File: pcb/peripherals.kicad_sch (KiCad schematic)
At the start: 30 parts, among them J2 Conn_01x24_MountingPin, J3 Conn_02x10_Odd_Even, U4 TLV74328PDBVR, U5 NRF24L01_Breakout, U6 TLV74315PDBVR, U7 BMI270, U8 HYCW110-TF10-180B

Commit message: [pcb] invented the cutting edge, extremely innovative monke and ddg connectors
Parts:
- removed J3: Conn_02x10_Odd_Even, Connector_PinHeader_2.54mm:PinHeader_2x10_P2.54mm_Vertical, symbol Connector_Generic:Conn_02x10_Odd_Even
- added J3: Conn_02x04_Odd_Even, symbol Connector_Generic:Conn_02x04_Odd_Even
- added J4: Conn_02x05_Odd_Even, symbol Connector_Generic:Conn_02x05_Odd_Even
- added SW5: SW_Slide_DPDT, symbol Switch:SW_Slide_DPDT
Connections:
- net +3.3V: now also J3.2 (Pin_2), J4.2 (Pin_2)
- net GND: now also J3.4 (Pin_4), J4.4 (Pin_4)
- net IMU_SCL: now also SW5.1 (A)
- net IMU_SDA: now also SW5.6 (C)
- net RST: now also J3.8 (Pin_8)
- net SPI2_CLK: now also J4.10 (Pin_10)
- net SPI2_MISO: now also SW5.3 (C)
- net SPI2_MOSI: now also SW5.4 (A)
- net TCLK: now also J3.7 (Pin_7)
- net TDI: now also J3.3 (Pin_3)
- net TDO: now also J3.6 (Pin_6)
- net TMS: now also J3.5 (Pin_5)
- net TRST: now also J3.1 (Pin_1)
- new net DDG_MAGIC_1: J4.1 (Pin_1)
- new net DDG_MAGIC_2: J4.3 (Pin_3)
- new net DDG_MAGIC_3: J4.5 (Pin_5)
- new net DDG_MAGIC_4: J4.7 (Pin_7)
- new net DDG_MAGIC_5: J4.9 (Pin_9)
- new net MISO_SCL: J4.6 (Pin_6), SW5.2 (B)
- new net MOSI_SDA: J4.8 (Pin_8), SW5.5 (B)
- no-connect marks 13 -> 10
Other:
- note added: "DUCKDUCKGOOSE (Digital Unified Centralized Kibibit Device Universal Coding Knowledge Generic Operable Objective Service Extensible) Connector"
- note added: "MONKE (Magic Overengineered Nonsense for Kernel Experiments) Connector"
- note removed: "JTAG Connector"
- moved on the sheet: C29, C30, C32, R16, R17, R18, R19, R20, R21, R23, R24, U7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

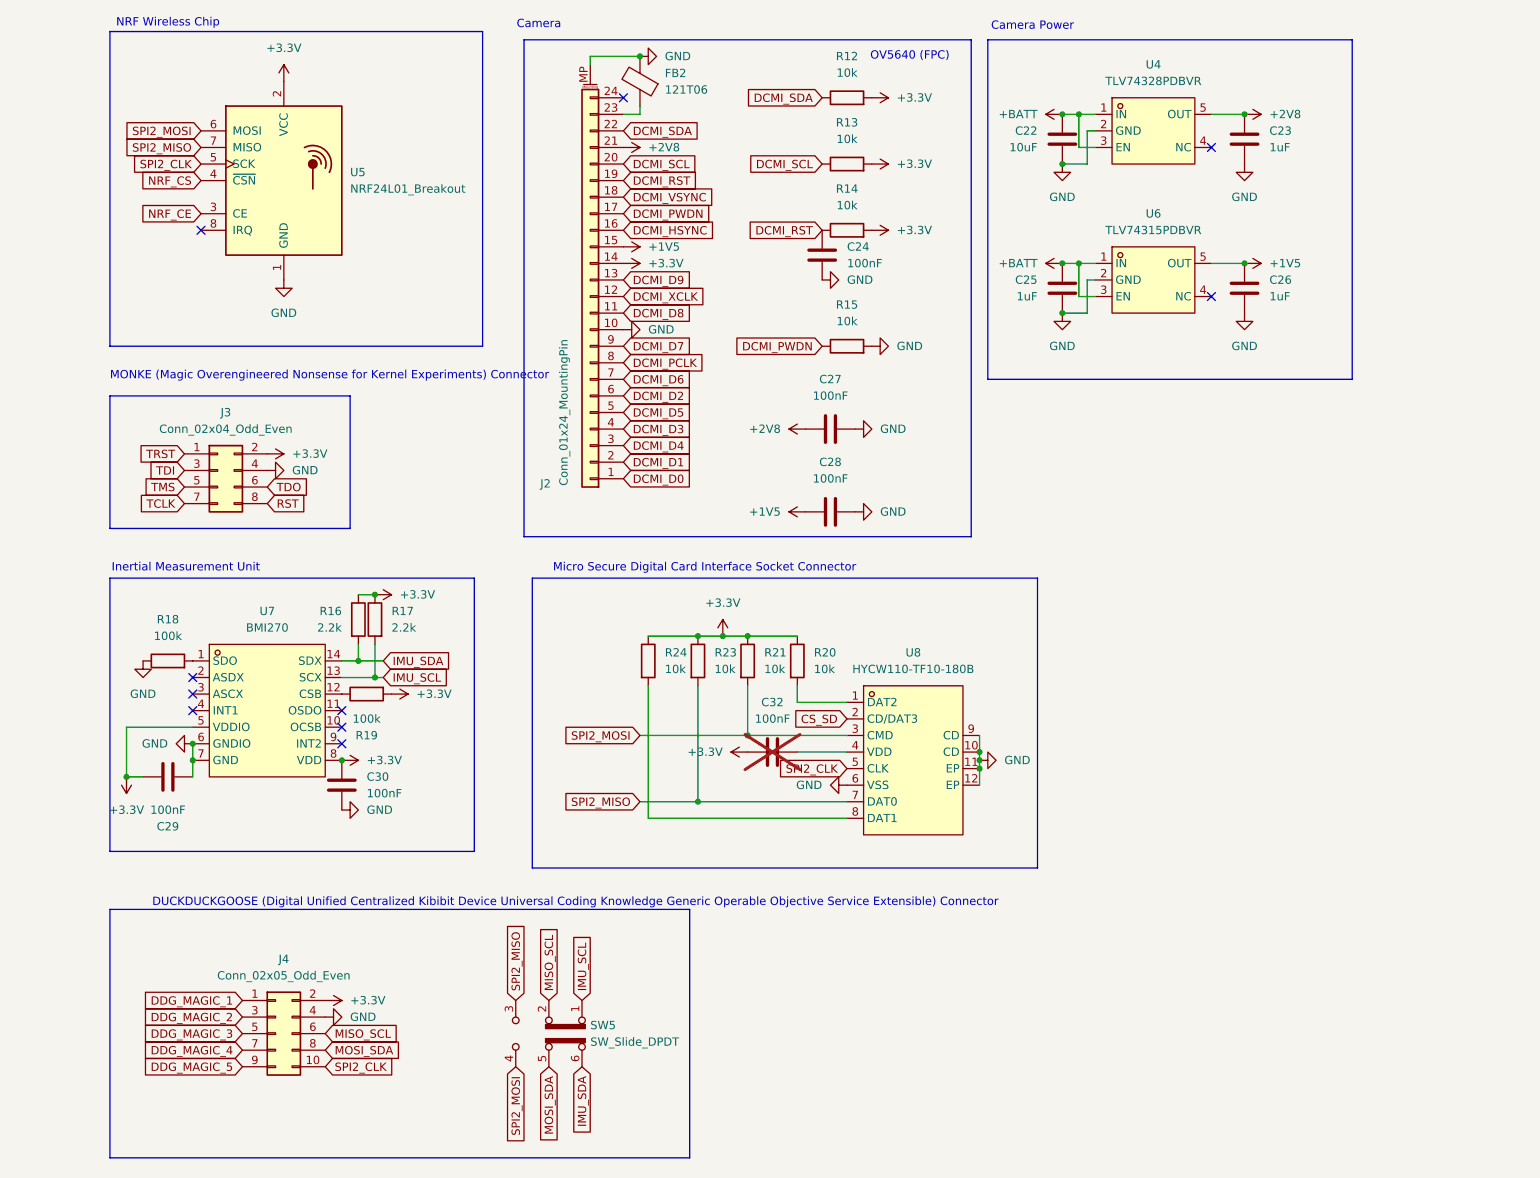
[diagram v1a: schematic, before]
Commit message: [pcb] changed switches to optimize pcb layout
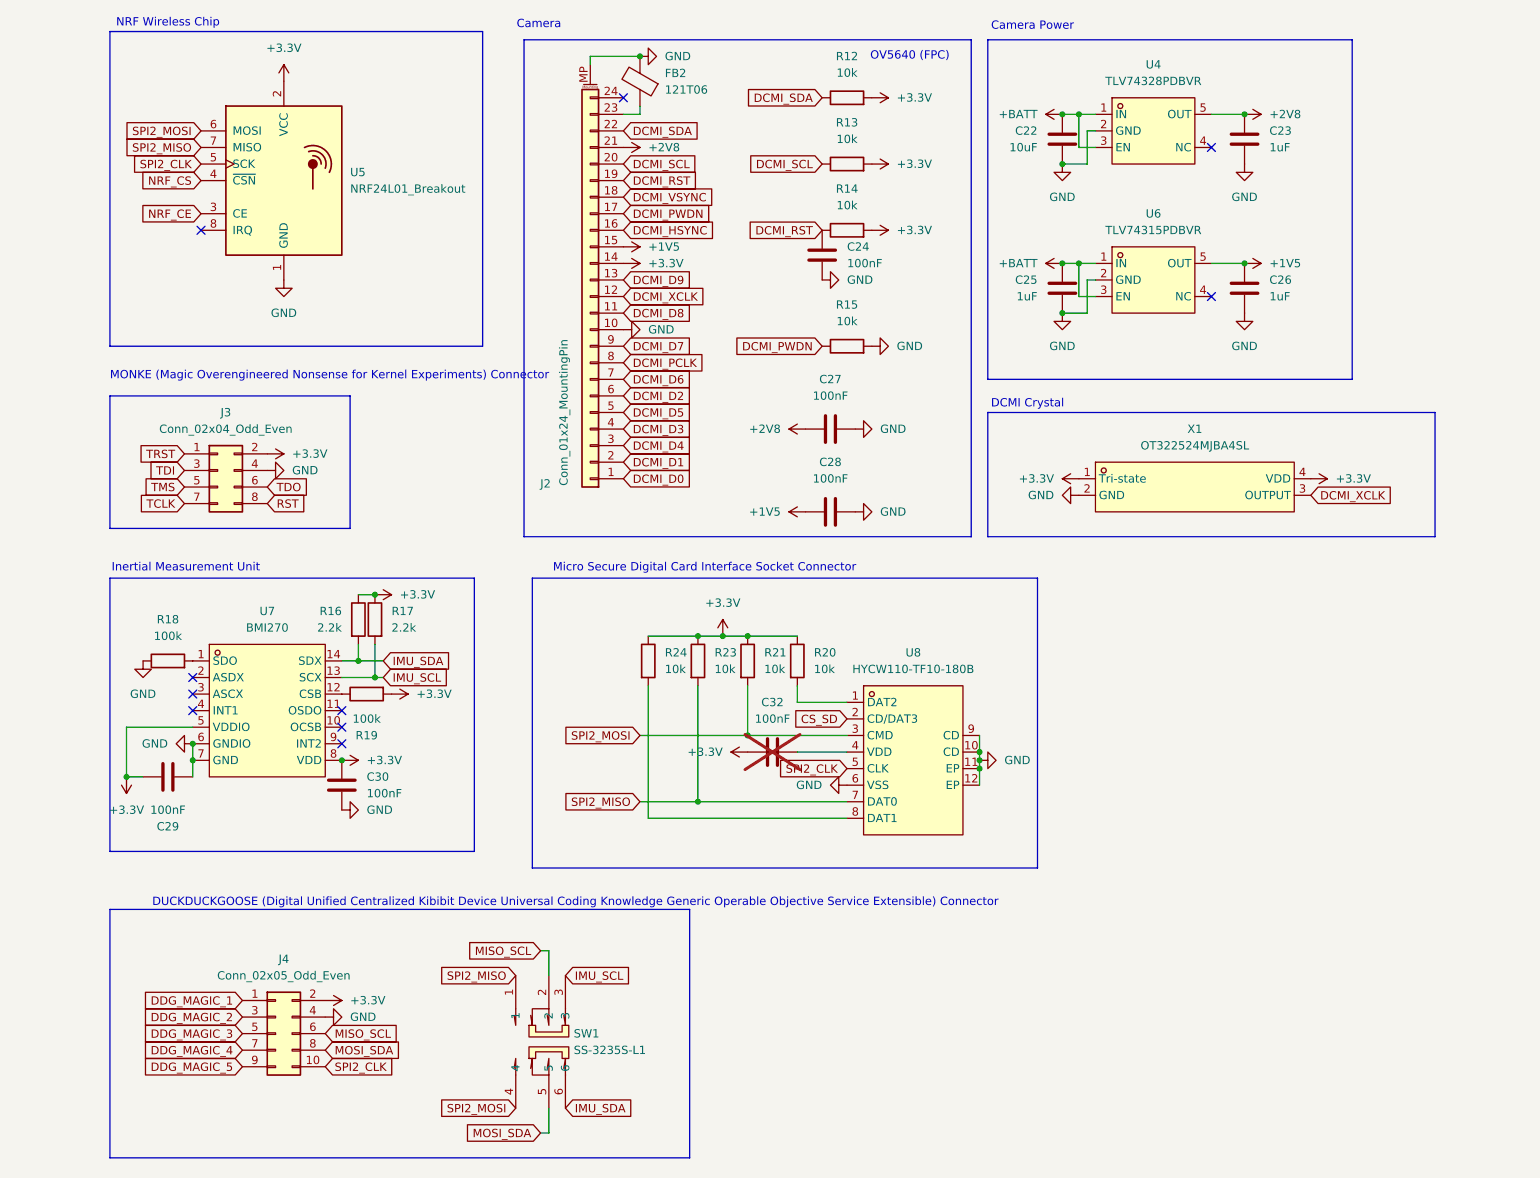
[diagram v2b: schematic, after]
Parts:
- removed SW5: SW_Slide_DPDT, symbol Switch:SW_Slide_DPDT
- added SW1: SS-3235S-L1, lcsc:SW-SMD_SS-3235S-LX, symbol lcsc:SS-3235S-L1
- added X1: OT322524MJBA4SL, Crystal:Crystal_SMD_3225-4Pin_3.2x2.5mm_HandSoldering, symbol lcsc:OT322524MJBA4SL
- J3: footprint (none) -> Connector_PinHeader_2.54mm:PinHeader_2x04_P2.54mm_Vertical
- J4: footprint (none) -> Connector_PinHeader_2.54mm:PinHeader_2x05_P2.54mm_Vertical
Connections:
- net +3.3V: now also X1.1 (Tri-state), X1.4 (VDD)
- net DCMI_XCLK: now also X1.3 (OUTPUT)
- net GND: now also X1.2 (GND)
- net IMU_SCL: now also SW1.3
- net IMU_SDA: now also SW1.6
- net MISO_SCL: now also SW1.2
- net MOSI_SDA: now also SW1.5
- net SPI2_MISO: now also SW1.1
- net SPI2_MOSI: now also SW1.4
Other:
- note added: "DCMI Crystal"

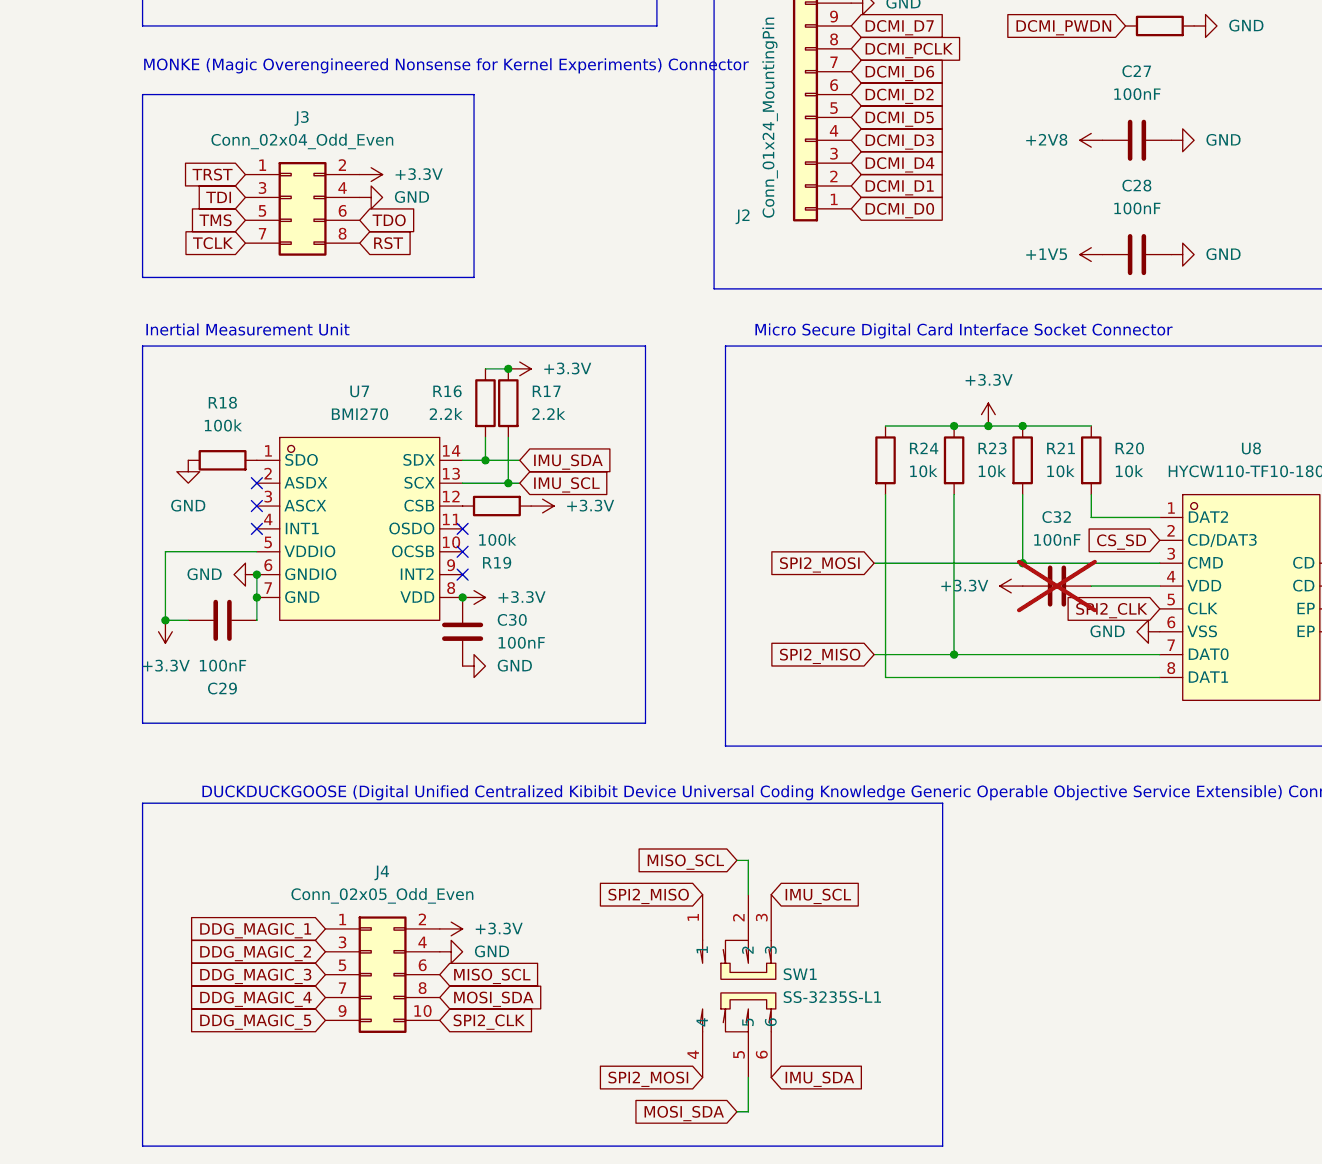
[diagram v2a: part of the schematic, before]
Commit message: [pcb] finish routing
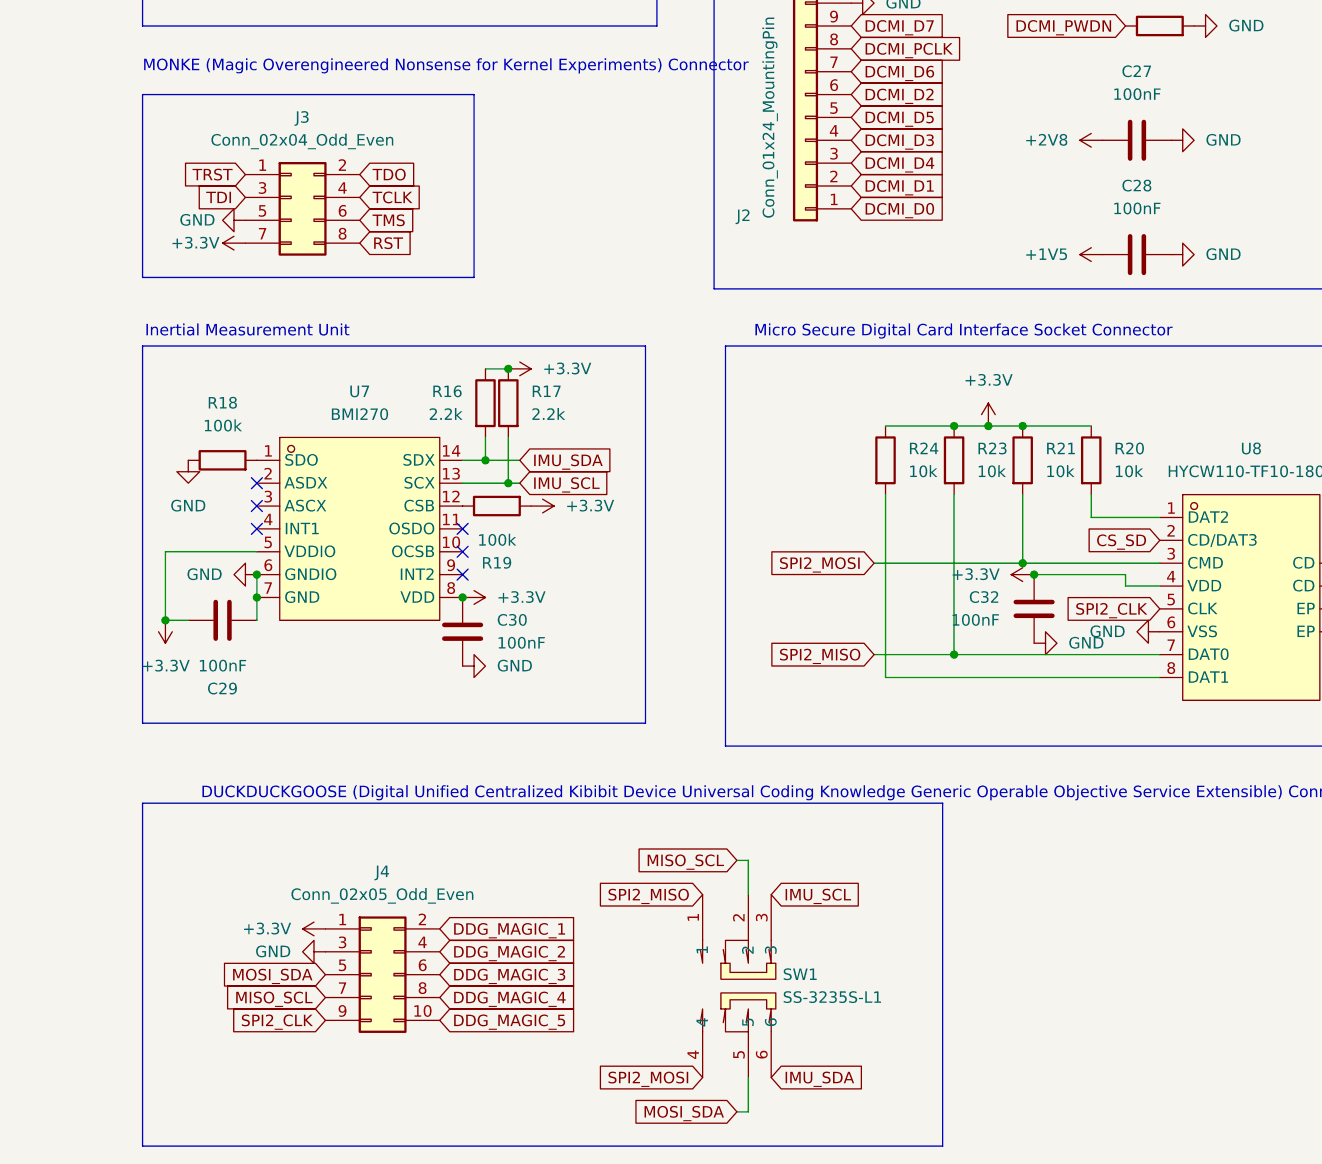
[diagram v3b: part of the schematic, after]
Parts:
- C32: now fitted
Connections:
- net +3.3V: now also J3.7 (Pin_7), J4.1 (Pin_1), U8.4 (VDD); no longer J3.2 (Pin_2), J4.2 (Pin_2)
- net DDG_MAGIC_1: now also J4.2 (Pin_2); no longer J4.1 (Pin_1)
- net DDG_MAGIC_2: now also J4.4 (Pin_4); no longer J4.3 (Pin_3)
- net DDG_MAGIC_3: now also J4.6 (Pin_6); no longer J4.5 (Pin_5)
- net DDG_MAGIC_4: now also J4.8 (Pin_8); no longer J4.7 (Pin_7)
- net DDG_MAGIC_5: now also J4.10 (Pin_10); no longer J4.9 (Pin_9)
- net GND: now also C32.2, J3.5 (Pin_5), J4.3 (Pin_3); no longer J3.4 (Pin_4), J4.4 (Pin_4)
- net MISO_SCL: now also J4.7 (Pin_7); no longer J4.6 (Pin_6)
- net MOSI_SDA: now also J4.5 (Pin_5); no longer J4.8 (Pin_8)
- net SPI2_CLK: now also J4.9 (Pin_9); no longer J4.10 (Pin_10)
- net TCLK: now also J3.4 (Pin_4); no longer J3.7 (Pin_7)
- net TDO: now also J3.2 (Pin_2); no longer J3.6 (Pin_6)
- net TMS: now also J3.6 (Pin_6); no longer J3.5 (Pin_5)

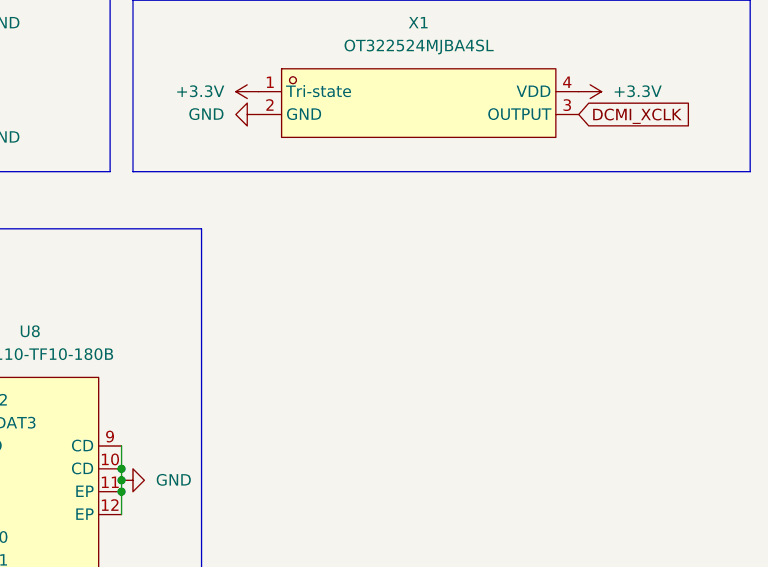
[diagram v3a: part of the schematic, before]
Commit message: [pcb] add status led
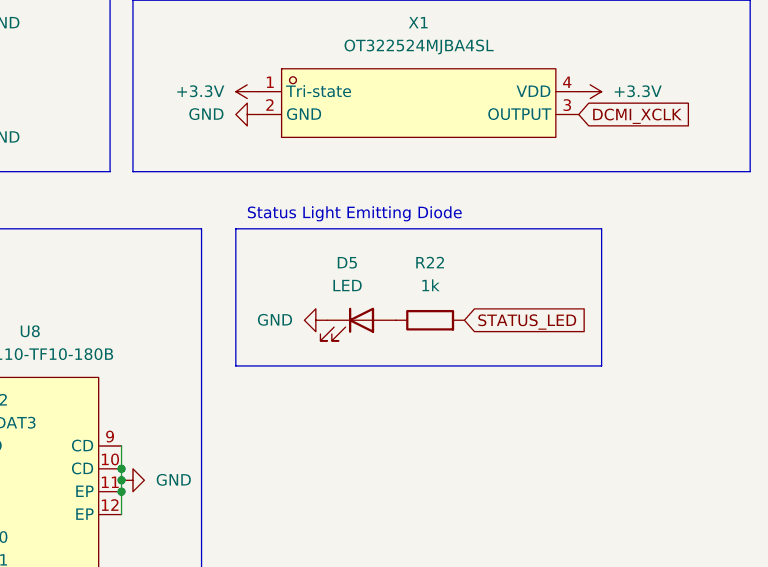
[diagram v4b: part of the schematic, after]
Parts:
- added D5: LED, LED_SMD:LED_0805_2012Metric, symbol Device:LED
- added R22: 1k, Resistor_SMD:R_0805_2012Metric, symbol Device:R
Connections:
- net GND: now also D5.1 (K)
- new net: D5.2 (A), R22.1
- new net STATUS_LED: R22.2
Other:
- note added: "Status Light Emitting Diode"
